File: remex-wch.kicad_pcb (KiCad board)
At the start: 4 copper layers, 83.8 x 22.9 mm, 99 parts, among them J1 Conn_01x16, J2 Conn_01x12, J3 USB_C_Receptacle_USB2.0_16P, J4 uSD SHOU HAN, J5 RJ45_Hanrun_HR911130C, J7 JST_PH, SW1 RESET, U1 CH32V307WCU6, U2 RTL8211F, U3 MS5351M, U4 HUSB311, U5 SY6820, U6 LW5233N11E, U7 LGS5500, U8 PY32F002AW15U, Y1 32.768kHz 12.5 pF Q13FC135000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, Y2 25 MHz 10 pF X322525MMB4SI

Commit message: small tweaks
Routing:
- net GND: track 105.8 -> 108.6 mm
- net /AUX_SWCLK: track 8.79 -> 8.03 mm

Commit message: more tweaks; prepare for adding accel
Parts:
- moved SW1 3.50 mm to (94.5, 134.5)
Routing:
- net /INT_I2C_SDA: track 39.0 -> 54.1 mm, vias 3 -> 4
- net /INT_I2C_SCL: track 44.2 -> 57.8 mm, vias 3 -> 4
- net GND: track 108.6 -> 113.1 mm
- net +3.3V: track 223.0 -> 221.9 mm
- net /~{RST}: track 86.2 -> 86.9 mm

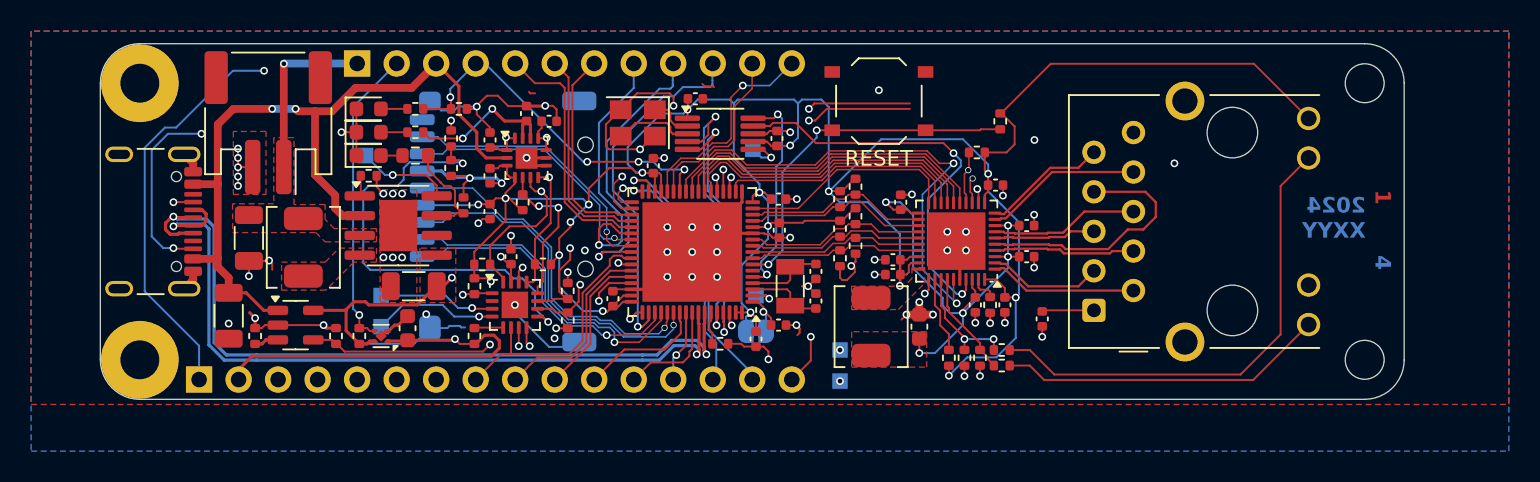
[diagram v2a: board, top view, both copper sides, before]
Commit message: add bonus accel
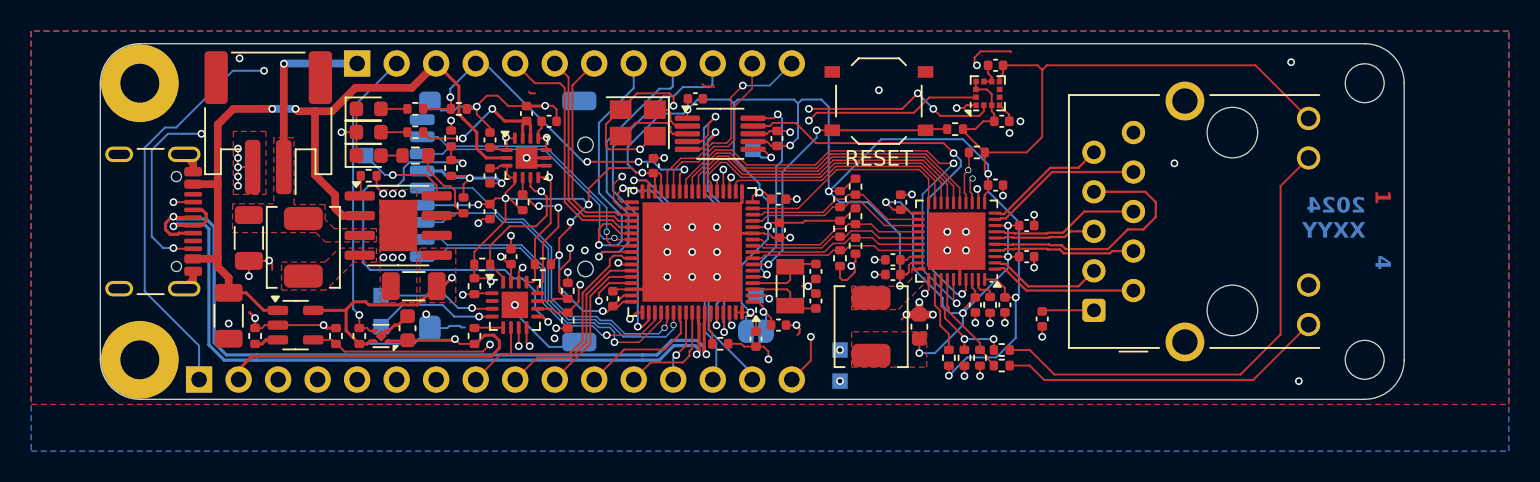
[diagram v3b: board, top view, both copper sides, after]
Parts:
- added C31: 0.1 uF, Capacitor_SMD:C_0402_1005Metric, F.Cu at (102.0, 132.2)
- added C32: 0.1 uF, Capacitor_SMD:C_0402_1005Metric, F.Cu at (102.4, 135.8)
- added U9: SC7A20, Package_LGA:LGA-12_2x2mm_P0.5mm, F.Cu at (101.5, 134.0)
- moved R33 2.94 mm to (99.4, 136.3), turned to 180 degrees
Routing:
- net +3.3V: track 221.9 -> 233.4 mm
- net GND: track 113.1 -> 120.4 mm, vias 69 -> 75
- net /INT_I2C_SDA: track 54.1 -> 60.2 mm, vias 4 -> 6
- net /INT_I2C_SCL: track 57.8 -> 62.3 mm
- net /~{RST}: track 86.9 -> 83.5 mm

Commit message: more tweaks
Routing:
- net GND: track 120.4 -> 123.1 mm
- net Net-(U2-DVDD10): track 30.3 -> 29.8 mm
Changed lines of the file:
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@@
 	)
 	(segment
+		(start 85.83 150.28)
+		(end 85.65 150.46)
+		(width 0.125)
+		(layer "F.Cu")
+		(net 2)
+	)
+	(segment
 		(start 54.245 138.74)
 		(end 53.31 138.74)
@@
 	)
 	(segment
+		(start 100.95 149)
+		(end 101.425 149)
+		(width 0.125)
+		(layer "F.Cu")
+		(net 2)
+	)
+	(segment
 		(start 105 148.98)
 		(end 105 149.65)
@@
 	)
 	(segment
+		(start 101.65 148.8)
+		(end 101.8 148.95)
+		(width 0.125)
+		(layer "F.Cu")
+		(net 2)
+	)
+	(segment
 		(start 92.95 145.25)
 		(end 92.95 145.5)
@@
 	)
 	(segment
+		(start 85.65 150.46)
+		(end 85.65 150.55)
+		(width 0.125)
+		(layer "F.Cu")
+		(net 2)
+	)
+	(segment
 		(start 70.25 139.78)
 		(end 69.5 139.78)
@@
 	)
 	(segment
+		(start 100.7 148.75)
+		(end 100.95 149)
+		(width 0.125)
+		(layer "F.Cu")
+		(net 2)
+	)
+	(segment
 		(start 90.45 146.87)
 		(end 90.42 146.87)
@@
 	)
 	(segment
+		(start 101.425 149)
+		(end 101.65 148.775)
+		(width 0.125)
+		(layer "F.Cu")
+		(net 2)
+	)
+	(segment
 		(start 100.65 132.05)
 		(end 100.65 131.7)
@@
 	)
 	(segment
+		(start 101.65 148.775)
+		(end 101.65 148.8)
+		(width 0.125)
+		(layer "F.Cu")
+		(net 2)
+	)
+	(segment
 		(start 99.5 134.95)
 		(end 99.95 134.95)
@@
 	)
 	(segment
+		(start 102.4 148.95)
+		(end 102.6 148.75)
+		(width 0.125)
+		(layer "F.Cu")
+		(net 2)
+	)
+	(segment
 		(start 53.31 138.74)
 		(end 53.3 138.75)
@@
 	)
 	(segment
+		(start 101.8 148.95)
+		(end 102.4 148.95)
+		(width 0.125)
+		(layer "F.Cu")
+		(net 2)
+	)
+	(segment
 		(start 89.4 149.1)
 		(end 89.4 149.2)
@@
 	)
 	(segment
-		(start 96.7 145.25)
-		(end 98.6 147.15)
+		(start 98.45 147)
+		(end 98.45 147.5)
 		(width 0.125)
 		(layer "B.Cu")
@@
 	)
 	(segment
-		(start 95.875 141)
-		(end 96.7 141.825)
-		(width 0.125)
-		(layer "B.Cu")
-		(net 8)
-	)
-	(segment
-		(start 99.075 148.125)
-		(end 99.9 148.125)
-		(width 0.125)
-		(layer "B.Cu")
-		(net 8)
-	)
-	(segment
-		(start 98.6 147.15)
-		(end 98.6 147.65)
+		(start 96.7 142.75)
+		(end 96.7 145.25)
 		(width 0.125)
 		(layer "B.Cu")
@@
 	)
 	(segment
-		(start 96.7 141.825)
-		(end 96.7 145.25)
+		(start 96.7 145.25)
+		(end 98.45 147)
 		(width 0.125)
 		(layer "B.Cu")
@@
 	(segment
 		(start 94.95 141)
-		(end 95.875 141)
+		(end 96.7 142.75)
 		(width 0.125)
 		(layer "B.Cu")
@@
 	)
 	(segment
-		(start 98.6 147.65)
+		(start 99.075 148.125)
+		(end 99.9 148.125)
+		(width 0.125)
+		(layer "B.Cu")
+		(net 8)
+	)
+	(segment
+		(start 98.45 147.5)
 		(end 99.075 148.125)
 		(width 0.125)
@@
 	)
 	(segment
-		(start 103.5 146.925)
-		(end 103.5 142.280285)
-		(width 0.125)
-		(layer "B.Cu")
-		(net 9)
-	)
-	(segment
 		(start 85.675 147.5)
 		(end 85.675 145.05)
@@
 	)
 	(segment
+		(start 103.3 142.080285)
+		(end 101.525 140.305285)
+		(width 0.125)
+		(layer "B.Cu")
+		(net 9)
+	)
+	(segment
 		(start 74.675 142.275)
 		(end 75.8 141.15)
@@
 	)
 	(segment
+		(start 101.525 140.305285)
+		(end 101.525 139.175)
+		(width 0.125)
+		(layer "B.Cu")
+		(net 9)
+	)
+	(segment
 		(start 82.2 135.05)
 		(end 81.95 135.3)
@@
 	)
 	(segment
+		(start 103.3 147.125)
+		(end 103.3 142.080285)
+		(width 0.125)
+		(layer "B.Cu")
+		(net 9)
+	)
+	(segment
 		(start 85.425 134.4)
 		(end 85.175 134.65)
@@
 	)
 	(segment
-		(start 103.5 142.280285)
-		(end 101.525 140.305285)
-		(width 0.125)
-		(layer "B.Cu")
-		(net 9)
-	)
-	(segment
-		(start 101.525 140.305285)
-		(end 101.525 139.175)
-		(width 0.125)
-		(layer "B.Cu")
-		(net 9)
-	)
-	(segment
 		(start 81.95 135.3)
 		(end 80.495134 135.3)
@@
 	)
 	(segment
-		(start 103.3 147.125)
-		(end 103.5 146.925)
-		(width 0.125)
-		(layer "B.Cu")
-		(net 9)
-	)
-	(segment
 		(start 75.5 148)
 		(end 76.75 148)
@@
 	)
 	(segment
-		(start 73.4 142.35)
-		(end 72.39 143.36)
+		(start 101.25 135.15)
+		(end 101.25 134.7625)
 		(width 0.125)
 		(layer "F.Cu")
@@
 	)
 	(segment
-		(start 101.25 135.15)
-		(end 101.25 134.7625)
+		(start 73.4 142.35)
+		(end 72.39 143.36)
 		(width 0.125)
 		(layer "F.Cu")
@@
 	)
 	(segment
+		(start 98.45 135.45)
+		(end 100.95 135.45)
+		(width 0.125)
+		(layer "F.Cu")
+		(net 70)
+	)
+	(segment
 		(start 84.5 148.7)
 		(end 84.55 148.75)
@@
 	)
 	(segment
-		(start 98.45 135.45)
-		(end 100.95 135.45)
-		(width 0.125)
-		(layer "F.Cu")
-		(net 70)
-	)
-	(segment
 		(start 73.3 139.4)
 		(end 72.6125 139.4)
@@
 	)
 	(segment
-		(start 82.1875 137.6)
-		(end 83.05 137.6)
+		(start 97.85 134.85)
+		(end 98.45 135.45)
 		(width 0.125)
 		(layer "F.Cu")
@@
 	)
 	(segment
-		(start 98 135)
-		(end 98.45 135.45)
+		(start 82.1875 137.6)
+		(end 83.05 137.6)
 		(width 0.125)
 		(layer "F.Cu")
@@
 	)
 	(via
-		(at 98 135)
+		(at 97.85 134.85)
 		(size 0.5)
 		(drill 0.3)
@@
 	)
 	(segment
-		(start 97 134)
-		(end 98 135)
+		(start 84.55 149.35)
+		(end 84.55 147.403554)
 		(width 0.125)
 		(layer "B.Cu")
@@
 	)
 	(segment
-		(start 84.55 149.35)
-		(end 84.55 147.403554)
+		(start 97 134)
+		(end 97.85 134.85)
 		(width 0.125)
 		(layer "B.Cu")
@@
 	)
 	(segment
-		(start 77.95 141)
-		(end 78.6125 141)
+		(start 100.5 141.0375)
+		(end 100.5 140.525)
 		(width 0.1)
 		(layer "F.Cu")
@@
 	)
 	(segment
-		(start 100.5 141.0375)
-		(end 100.5 140.467053)
+		(start 100.5 140.525)
+		(end 100.3 140.325)
 		(width 0.1)
 		(layer "F.Cu")
@@
 	)
 	(segment
-		(start 78.05 140.1)
-		(end 77.75 140.4)
+		(start 100.3 139.7)
+		(end 100.525 139.475)
 		(width 0.1)
 		(layer "F.Cu")
@@
 	)
 	(segment
-		(start 100.371 140.338053)
-		(end 100.371 139.629)
+		(start 77.95 141)
+		(end 78.6125 141)
 		(width 0.1)
 		(layer "F.Cu")
@@
 	)
 	(segment
-		(start 77.75 140.4)
-		(end 77.75 140.8)
+		(start 100.3 140.325)
+		(end 100.3 139.7)
 		(width 0.1)
 		(layer "F.Cu")
@@
 	)
 	(segment
-		(start 100.5 140.467053)
-		(end 100.371 140.338053)
+		(start 78.05 140.1)
+		(end 77.75 140.4)
 		(width 0.1)
 		(layer "F.Cu")
@@
 	)
 	(segment
-		(start 100.371 139.629)
-		(end 100.525 139.475)
+		(start 77.75 140.4)
+		(end 77.75 140.8)
 		(width 0.1)
 		(layer "F.Cu")
